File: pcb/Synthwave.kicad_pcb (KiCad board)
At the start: 2 copper layers, 72.4 x 112.8 mm, 62 parts, among them J1 Barrel_Jack_Switch, J10 FLOAT2 GPIO39, J11 ELECTRODES Conn_01x04_Socket, J2 PUMP1 VALVE1 VALVE4 Conn_01x06_Socket, J3 CO2 SENSOR SDA, J4 PUMP2 VALVE2 VALVE3 Conn_01x06_Socket, J5 PH2 ADC3, J6 PH1 ADC4, J7 VAC1 VAC2 Conn_01x04_Socket, J8 REL1 REL2 Conn_01x04_Socket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

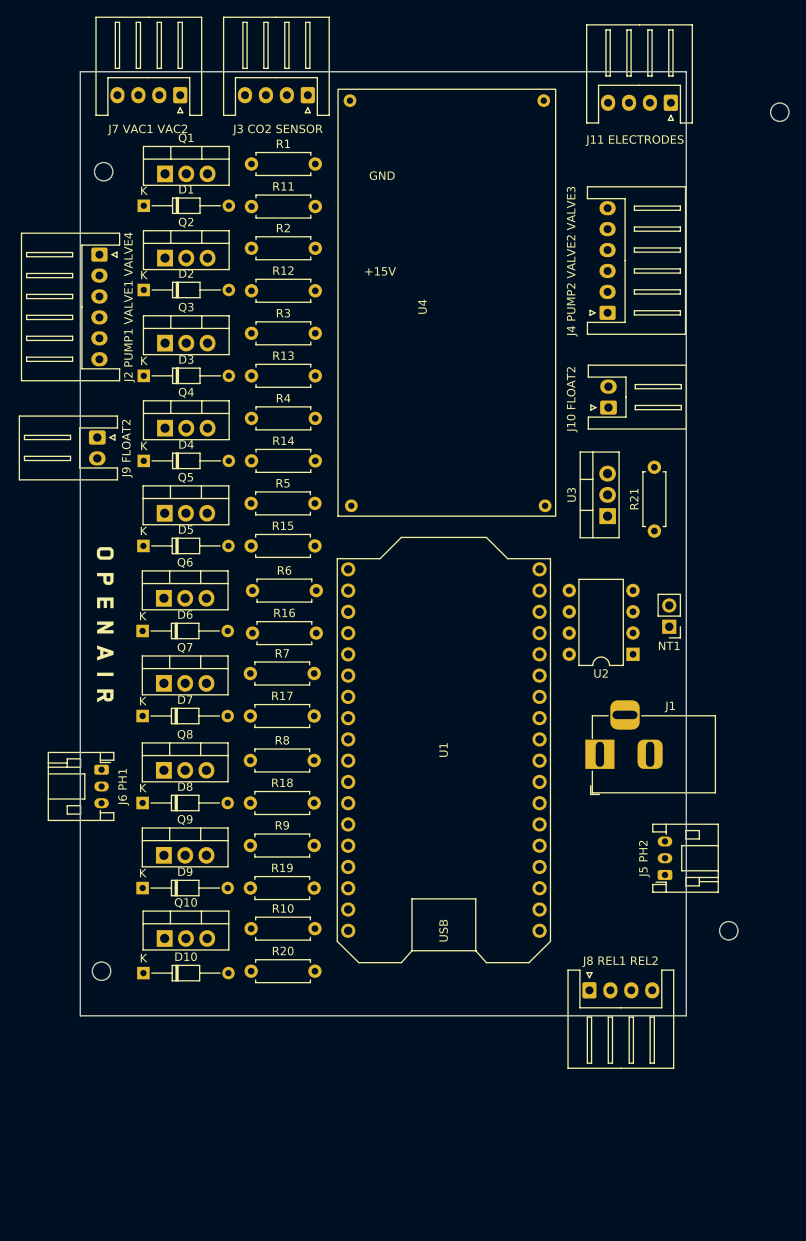
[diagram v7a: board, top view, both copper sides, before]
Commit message: Combine JST connectors
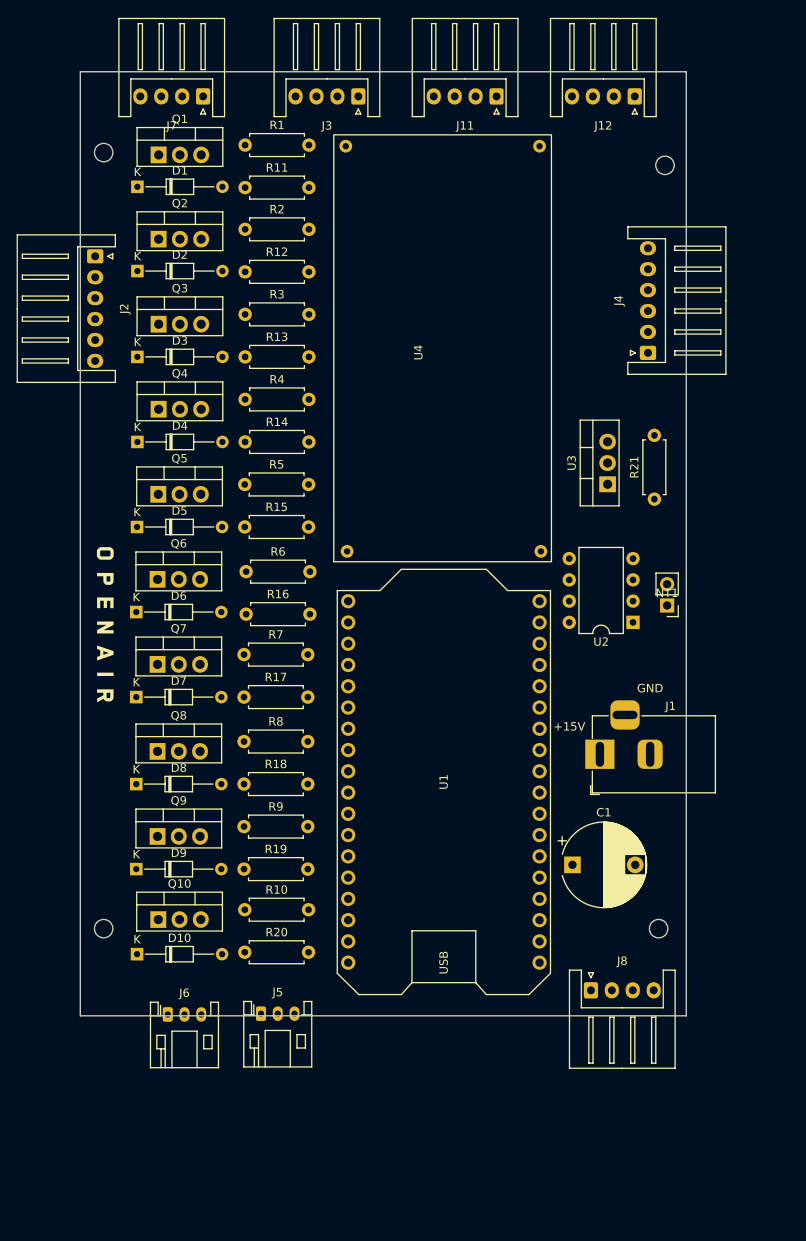
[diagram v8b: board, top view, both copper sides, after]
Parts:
- removed J10 FLOAT2: GPIO39, Connector_JST:JST_XH_S2B-XH-A_1x02_P2.50mm_Horizontal
- removed J11 ELECTRODES: Conn_01x04_Socket, Connector_JST:JST_XH_S4B-XH-A_1x04_P2.50mm_Horizontal
- removed J2 PUMP1 VALVE1 VALVE4: Conn_01x06_Socket, Connector_JST:JST_XH_S6B-XH-A_1x06_P2.50mm_Horizontal
- removed J3 CO2 SENSOR: SDA, Connector_JST:JST_XH_S4B-XH-A_1x04_P2.50mm_Horizontal
- removed J4 PUMP2 VALVE2 VALVE3: Conn_01x06_Socket, Connector_JST:JST_XH_S6B-XH-A_1x06_P2.50mm_Horizontal
- removed J5 PH2: ADC3, Connector_JST:JST_PH_S3B-PH-K_1x03_P2.00mm_Horizontal
- removed J6 PH1: ADC4, Connector_JST:JST_PH_S3B-PH-K_1x03_P2.00mm_Horizontal
- removed J7 VAC1 VAC2: Conn_01x04_Socket, Connector_JST:JST_XH_S4B-XH-A_1x04_P2.50mm_Horizontal
- removed J8 REL1 REL2: Conn_01x04_Socket, Connector_JST:JST_XH_S4B-XH-A_1x04_P2.50mm_Horizontal
- removed J9 FLOAT2: GPIO26, Connector_JST:JST_XH_S2B-XH-A_1x02_P2.50mm_Horizontal
- added C1: C_Polarized, Capacitor_THT:CP_Radial_D10.0mm_P7.50mm, F.Cu at (75.3, 106.7)
- added J11: Conn_01x04_Socket, Connector_JST:JST_XH_S4B-XH-A_1x04_P2.50mm_Horizontal, F.Cu at (66.2, 14.9)
- added J12: Conn_01x04_Socket, Connector_JST:JST_XH_S4B-XH-A_1x04_P2.50mm_Horizontal, F.Cu at (82.7, 14.9)
- added J2: Conn_01x06_Socket, Connector_JST:JST_XH_S6B-XH-A_1x06_P2.50mm_Horizontal, F.Cu at (18.3, 34.0)
- added J3: SDA, Connector_JST:JST_XH_S4B-XH-A_1x04_P2.50mm_Horizontal, F.Cu at (49.7, 14.9)
- added J4: Conn_01x06_Socket, Connector_JST:JST_XH_S6B-XH-A_1x06_P2.50mm_Horizontal, F.Cu at (84.3, 45.5)
- added J5: ADC3, Connector_JST:JST_PH_S3B-PH-K_1x03_P2.00mm_Horizontal, F.Cu at (38.1, 124.5)
- added J6: ADC4, Connector_JST:JST_PH_S3B-PH-K_1x03_P2.00mm_Horizontal, F.Cu at (27.0, 124.5)
- added J7: Conn_01x04_Socket, Connector_JST:JST_XH_S4B-XH-A_1x04_P2.50mm_Horizontal, F.Cu at (31.2, 14.9)
- added J8: Conn_01x04_Socket, Connector_JST:JST_XH_S4B-XH-A_1x04_P2.50mm_Horizontal, F.Cu at (77.5, 121.7)
- moved H4 15.1 mm to (86.4, 23.1)
- moved H3 8.39 mm to (85.6, 114.3)
- moved U4 5.47 mm to (46.8, 70.5)
- moved H2 5.09 mm to (19.3, 114.3)
- moved R21 3.81 mm to (85.1, 63.0)
- moved U1 3.81 mm to (59.9, 96.8)
- moved U2 3.81 mm to (82.5, 77.7)
- moved U3 3.81 mm to (79.5, 61.2)
- moved NT1 2.55 mm to (86.6, 75.7)
- moved R2 2.39 mm to (36.2, 30.8)
- moved D1 2.39 mm to (23.3, 25.7)
- moved D10 2.39 mm to (23.3, 117.3)
- moved D2 2.39 mm to (23.3, 35.7)
- moved D3 2.39 mm to (23.3, 46.0)
- moved D4 2.39 mm to (23.3, 56.2)
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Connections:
- R21 pad 1: Net-(J10-Pin_1) -> Net-(J3-Pin_3)
- R21 pad 2: Net-(J3-Pin_3) -> Net-(J12-Pin_3)
- U1 pad 5: Net-(J10-Pin_1) -> Net-(J12-Pin_3)
